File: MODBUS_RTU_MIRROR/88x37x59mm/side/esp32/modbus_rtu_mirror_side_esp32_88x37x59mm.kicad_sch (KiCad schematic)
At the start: 40 parts, among them J1 Conn_01x04_Male, J2 Conn_01x04_Male, J3 Conn_01x06_Male, J4 Conn_01x07_Male, J5 Conn_01x07_Male, SW1 SW_Push, U1 ESP32-WROOM-32, U2 TXS0108EPW, U3 AMS1117-3.3, U4 DS3231MZ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

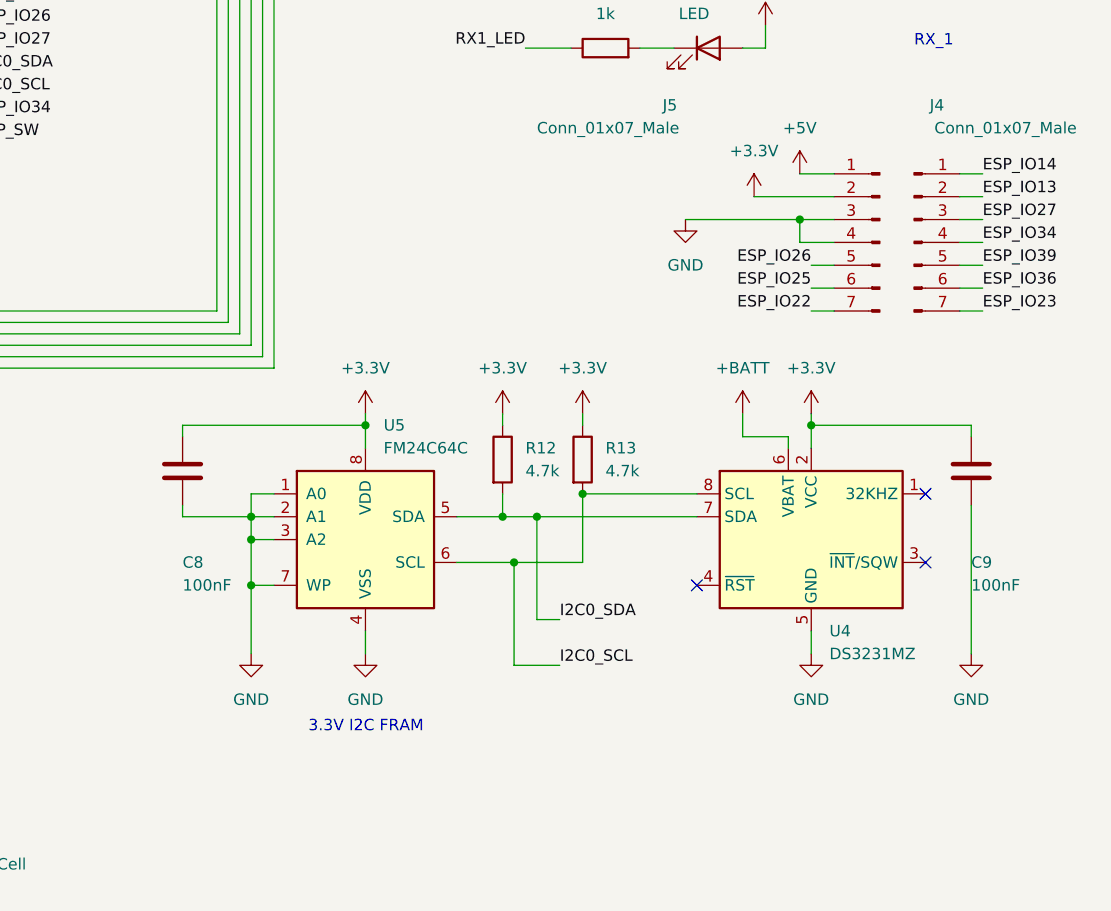
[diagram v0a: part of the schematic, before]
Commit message: added mech support pins for expansion board
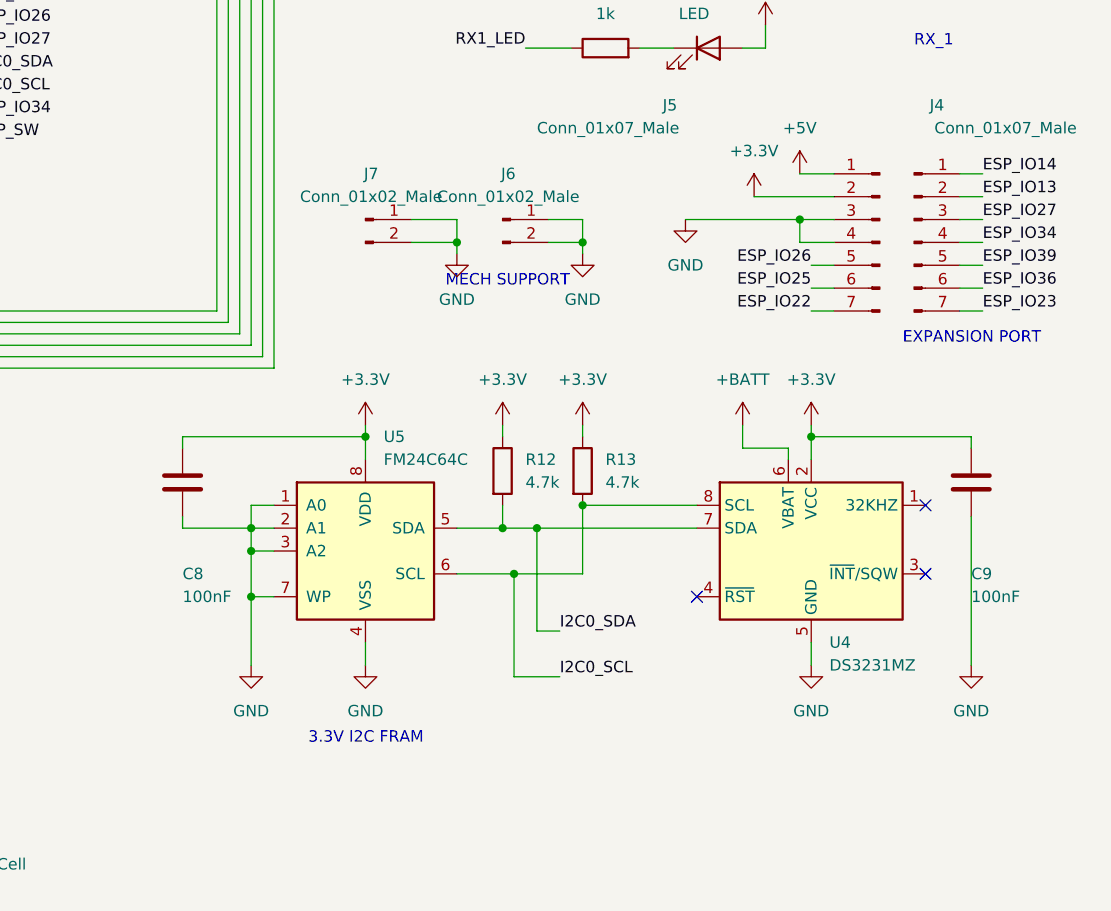
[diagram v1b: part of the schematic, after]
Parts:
- added J6, J7: Conn_01x02_Male, Connector_PinHeader_1.00mm:PinHeader_1x02_P1.00mm_Vertical, symbol Connector:Conn_01x02_Male
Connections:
- net GND: now also J6.1 (Pin_1), J6.2 (Pin_2), J7.1 (Pin_1), J7.2 (Pin_2)
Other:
- note added: "EXPANSION PORT"
- note added: "MECH SUPPORT"
- moved on the sheet: C8, C9, R12, R13, U4, U5
